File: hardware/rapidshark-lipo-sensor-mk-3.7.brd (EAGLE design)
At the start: 30.5 x 17.8 mm, 26 parts, among them Q1 IRLML2244, Q2 IRLML2502, Q3 IRLML2244, Q4 IRLML2502, Q5 IRLML2244, Q6 IRLML2502, U1 Tiny84

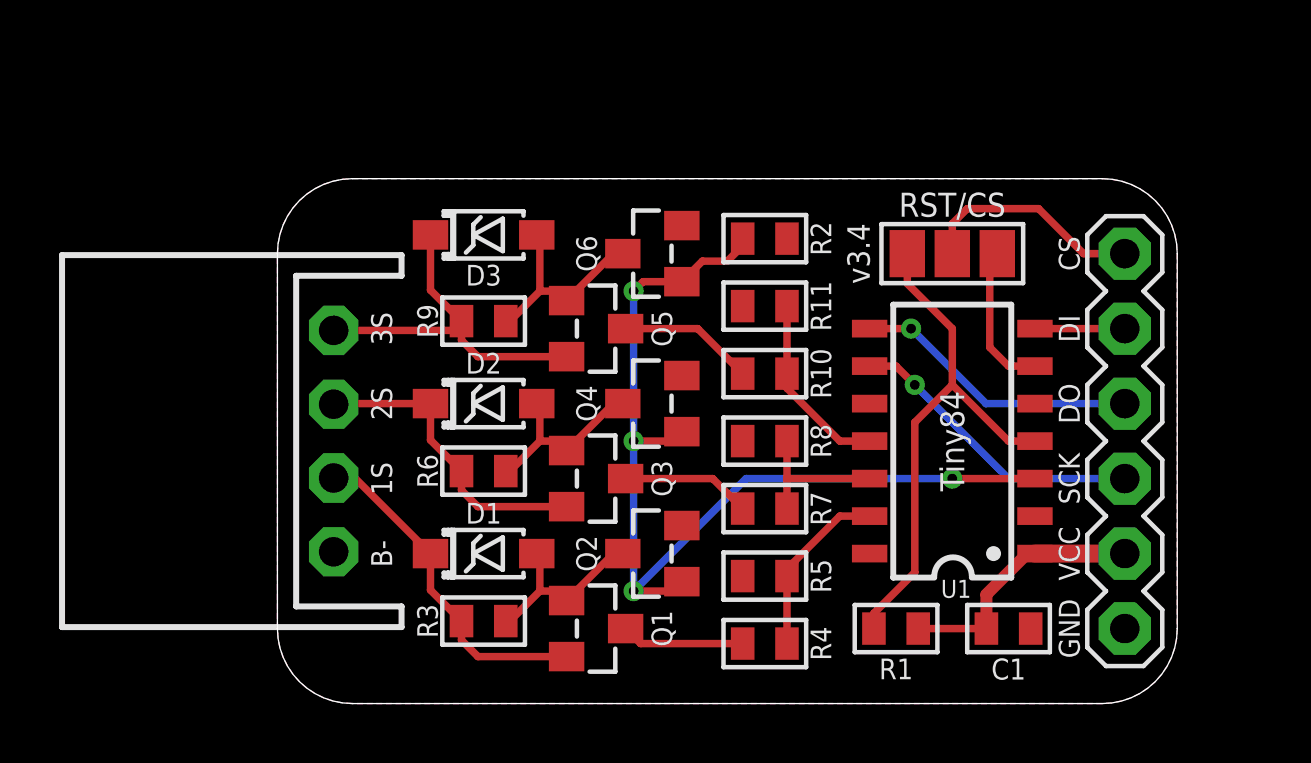
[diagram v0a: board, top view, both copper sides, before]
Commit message: lipo sensors suck
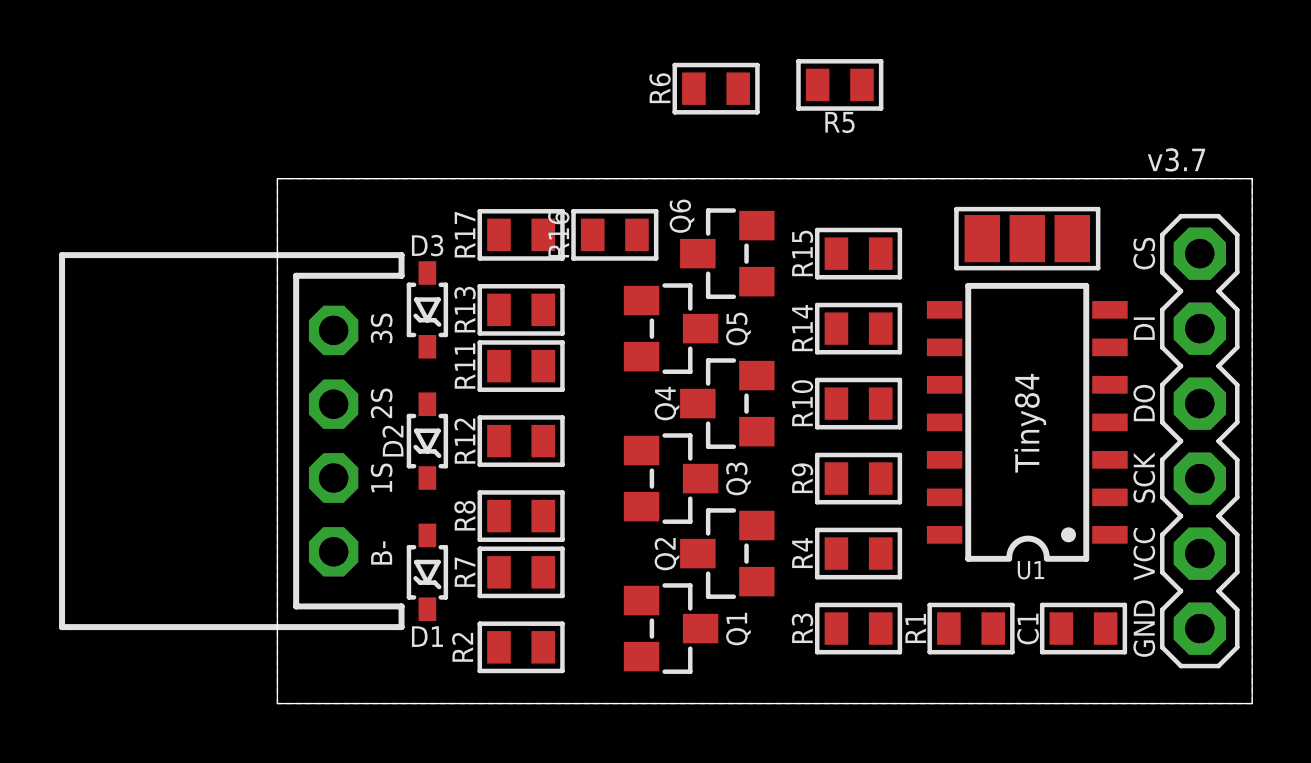
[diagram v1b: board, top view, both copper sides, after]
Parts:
- added R12, R17: 100R, a_parts:R0603-TIGHTER
- added R13: 1K, a_parts:R0603-TIGHTER
- added R14: 36K, a_parts:R0603-TIGHTER
- added R15: 10K, a_parts:R0603-TIGHTER
- added R16: 2K2, a_parts:R0603-TIGHTER
- D1, D2, D3: value MMSZ5240 -> MM3Z6V2T1G; device a_parts:SOD123-ZENER -> a_parts:SOD323-ZENNER
- Q1, Q3, Q5: value IRLML2244 -> BSH203
- Q2, Q4, Q6: value IRLML2502 -> MMBT2222A
- R1: value 100K -> 10K
- R10: value 36K -> 10K
- R11, R8: value 10K -> 1K
- R2: value 100K -> 1K
- R3: value 100K -> 4K7
- R4: value 4K7 -> 10K
- R6: value 100K -> 100R
- R7: value 22K -> 100R
- R9: value 100K -> 22K
- moved R5 16.8 mm to (19.1, 21.0), turned to 180 degrees
- moved R2 16.1 mm to (8.26, 1.91)
- moved R6 15.2 mm to (14.9, 20.8)
- moved R9 13.8 mm to (19.7, 7.62), turned to 180 degrees
- moved R3 12.7 mm to (19.7, 2.54), turned to 180 degrees
- moved R8 8.64 mm to (8.26, 6.35)
- moved R7 8.53 mm to (8.26, 4.45)
- moved R11 8.50 mm to (8.26, 11.4), turned to 180 degrees
- moved R4 4.40 mm to (19.7, 5.08), turned to 0 degrees
- moved R10 3.33 mm to (19.7, 10.2), turned to 0 degrees
- moved D3 3.17 mm to (5.08, 13.3), turned to 270 degrees
- moved U1 2.62 mm to (25.4, 9.53)
- moved RST/CS 2.59 mm to (25.4, 15.7)
- moved R1 2.54 mm to (23.5, 2.54)
- moved Q1 2.54 mm to (13.3, 2.54)
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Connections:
- removed net N$4: D1.A, Q1.1, Q2.3, R3.2
- new net EN_DIV_RLY: Q2.1, Q4.1, Q6.1, R6.1
- new net N$1: Q4.3, R11.1
- new net N$10: Q1.1, R7.1
- new net N$11: Q3.1, R12.1
- new net N$12: Q5.1, R17.1
- new net N$8: Q6.3, R16.1
- new net N$9: D1.A, Q2.3, R2.2, R7.2
- net CELL1+: now also R2.1; no longer R3.1
- net CELL2+: now also R8.1; no longer R6.1
- net CELL3+: now also R13.1; no longer R9.1
- net EN_DIV: now also R5.2, R6.2; no longer Q2.1, Q4.1, Q6.1, R2.2
- net GND: now also R10.1, R15.1, R4.1; no longer R11.1, R2.1, R8.1
- net N$2: now also R9.2; no longer R7.2
- net N$3: now also R14.2; no longer R10.2
- net N$5: now also R11.2, R12.2, R8.2; no longer Q3.1, Q4.3, R6.2
- net N$6: now also R3.2; no longer R4.2
- net N$7: now also R13.2, R16.2, R17.2; no longer Q5.1, Q6.3, R9.2
- net VDIV1: now also R3.1, R4.2; no longer R4.1, R5.2
- net VDIV2: now also R10.2, R9.1; no longer R7.1, R8.2
- net VDIV3: now also R14.1, R15.2; no longer R10.1, R11.2
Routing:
- net EN_DIV: track 33.4 -> 0.00 mm, vias 4 -> 0
- net RESET: track 18.0 -> 0.00 mm
- net CELL3+: track 12.3 -> 0.00 mm
- net CELL1+: track 11.5 -> 0.00 mm
- net CELL2+: track 10.4 -> 0.00 mm
- net SCK: track 10.2 -> 0.00 mm, vias 1 -> 0
- net DO/MISO: track 9.69 -> 0.00 mm, vias 1 -> 0
- net VCC: track 8.73 -> 0.00 mm
- net RST/CS: track 7.70 -> 0.00 mm
- net N$7: track 7.13 -> 0.00 mm
- net N$5: track 6.49 -> 0.00 mm
- net N$4: track 6.49 -> 0.00 mm
- net VDIV3: track 6.32 -> 0.00 mm
- net VDIV1: track 6.07 -> 0.00 mm
- net VDIV2: track 5.09 -> 0.00 mm
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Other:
- board size 30.5 x 17.8 mm -> 33 x 17.8 mm

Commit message: oh hey more hardware fails
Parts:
- removed R12, R17, R7: 100R, a_parts:R0603-TIGHTER
- moved R5 4.99 mm to (17.8, 16.1)
- moved R6 4.84 mm to (13.7, 16.1)
- moved Q1 3.24 mm to (10.2, 3.17)
- moved Q3 3.24 mm to (10.2, 6.99)
- moved Q5 3.24 mm to (10.2, 12.1), turned to 180 degrees
- moved R15 2.44 mm to (17.8, 13.7)
- moved R10 2.40 mm to (17.7, 8.89)
- moved R14 2.36 mm to (17.8, 11.3)
- moved Q6 2.29 mm to (14.0, 13.3), turned to 270 degrees
- moved JP2 2.16 mm to (29.1, 8.89)
- moved R4 2.16 mm to (17.8, 4.06)
- moved R9 2.16 mm to (17.8, 6.60)
- moved R3 2.10 mm to (17.8, 1.65)
- moved U1 2.01 mm to (23.5, 8.89)
- moved RST/CS 1.97 mm to (23.5, 15.2)
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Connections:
- removed net N$10: Q1.1, R7.1
- removed net N$11: Q3.1, R12.1
- removed net N$12: Q5.1, R17.1
- net N$5: now also Q3.1; no longer R12.2
- net N$7: now also Q5.1; no longer R17.2
- net N$9: now also Q1.1; no longer R7.2
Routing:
- net EN_DIV: track 0.00 -> 21.1 mm, vias 0 -> 2
- net EN_DIV_RLY: track 0.00 -> 20.7 mm, vias 0 -> 3
- net RESET: track 0.00 -> 17.4 mm
- net CELL1+: track 0.00 -> 11.4 mm
- net SCK: track 0.00 -> 9.97 mm, vias 0 -> 1
- net DO/MISO: track 0.00 -> 9.44 mm, vias 0 -> 1
- net CELL2+: track 0.00 -> 9.32 mm
- net N$9: track 0.00 -> 9.19 mm
- net N$8: track 0.00 -> 8.89 mm, vias 0 -> 2
- net CELL3+: track 0.00 -> 8.69 mm
- net VCC: track 0.00 -> 8.47 mm
- net N$5: track 0.00 -> 8.05 mm
- net N$7: track 0.00 -> 7.67 mm
- net N$3: track 0.00 -> 7.19 mm
- net RST/CS: track 0.00 -> 7.05 mm
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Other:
- board size 33 x 17.8 mm -> 30.5 x 17.8 mm
